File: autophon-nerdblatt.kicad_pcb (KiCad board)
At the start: 2 copper layers, 265 x 50.6 mm, 96 parts, among them J1 Conn_01x06_Female, J101 board-edge-connector, Q300 BSS84, Q301 BSS84, Q302 BSS84, Q303 BSS84, Q304 BSS84, Q305 BSS84, SW1 SW_Push, SW2 SW_Push, U101 LM1117-3.3, U102 LM2594M-5.0, U201 SN74LV1T34, U202 SN74LV1T34, U203 74AHCT595, U204 SN74LV1T34, U205 74AHCT595, U206 ESP32-WROOM-32, U207 74AHCT595, U300 L298HN, U301 L298HN, U302 L298HN

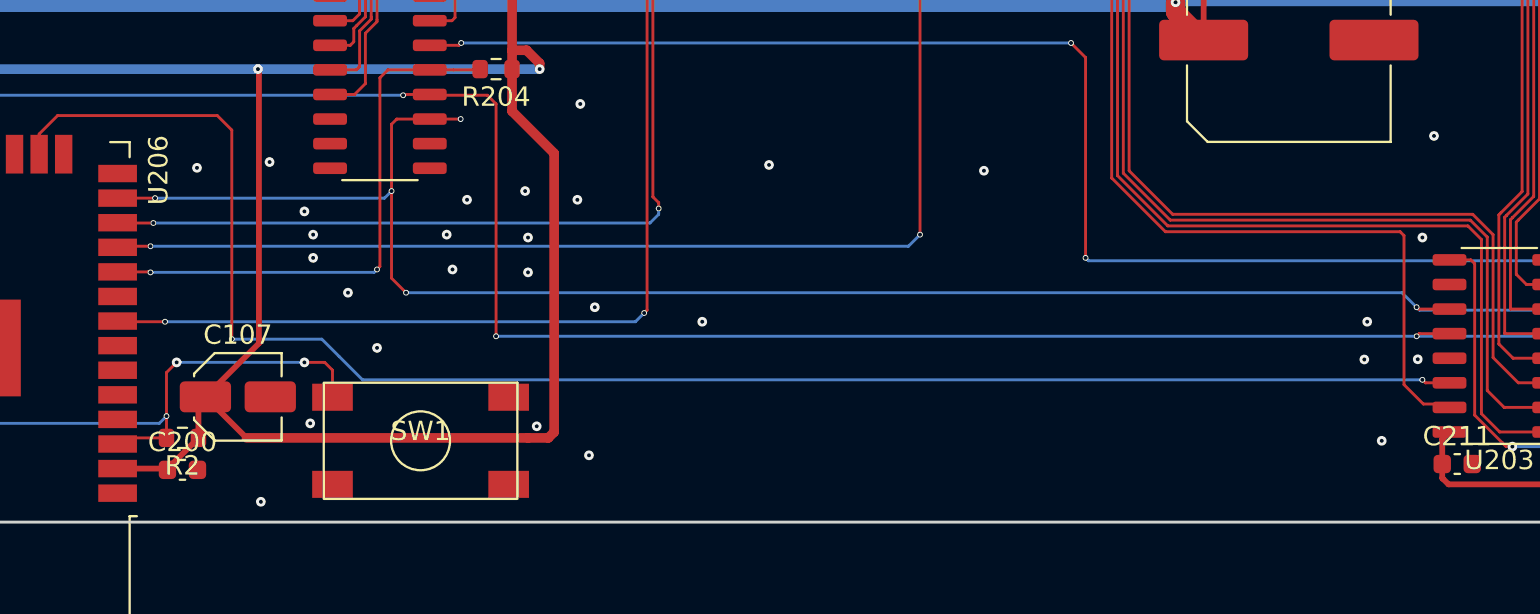
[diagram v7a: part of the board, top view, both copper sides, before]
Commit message: Add external connector, and swapped ESP pins.
Pins for motor enable, hallsensor enable and
readback of hall-sensors have been moved to
more appropriate pins.

(2 to input only, and the enable pins to
 gpios with no interesting auxiliary functions)
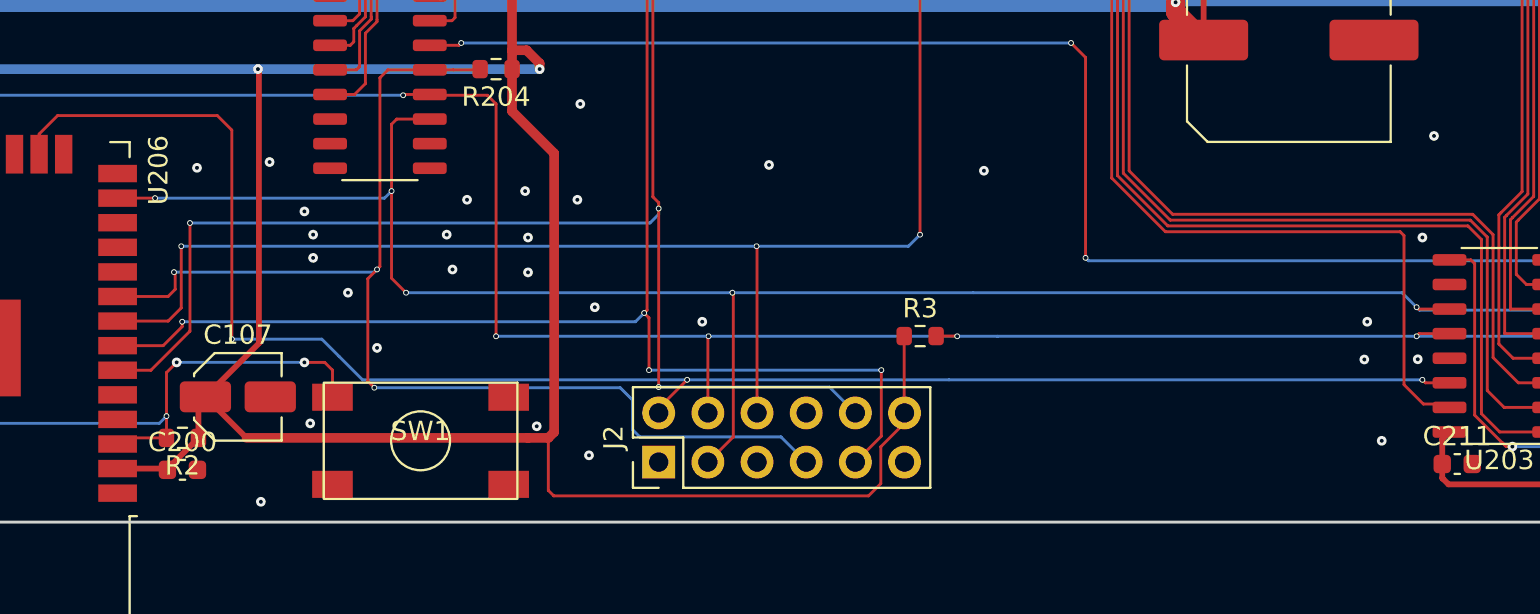
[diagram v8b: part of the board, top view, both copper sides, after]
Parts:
- added J2: Conn_02x06_Odd_Even, Connector_PinHeader_2.54mm:PinHeader_2x06_P2.54mm_Vertical, F.Cu at (225.0, 125.0)
- added R3: 10k, Resistor_SMD:R_0603_1608Metric, F.Cu at (238.5, 118.5)
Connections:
- net Net-(U206-Pad27) renamed /ESP32_Shiftregs/UART2_RXD
- net Net-(U206-Pad28) renamed /ESP32_Shiftregs/UART2_TXD
- net Net-(U206-Pad29) renamed /ESP32_Shiftregs/~VSPICS0~
- net Net-(U206-Pad30) renamed /ESP32_Shiftregs/VSPICLK
- net Net-(U206-Pad31) renamed /ESP32_Shiftregs/VSPIQ
- net Net-(U206-Pad33) renamed /ESP32_Shiftregs/I2C_SDA
- net Net-(U206-Pad36) renamed /ESP32_Shiftregs/I2C_SCL
- net Net-(U206-Pad37) renamed /ESP32_Shiftregs/VSPID
- net SPI_CIPO renamed /ESP32_Shiftregs/SPI_CIPO
- net SPI_CLK renamed /ESP32_Shiftregs/SPI_CLK
- net SPI_COPI renamed /ESP32_Shiftregs/SPI_COPI
- J101 pad 12A: no_connect_96 -> no_connect_95
- J101 pad 13A: no_connect_97 -> no_connect_96
- J101 pad 14A: no_connect_98 -> no_connect_97
- J101 pad 15A: no_connect_99 -> no_connect_98
- J101 pad 15B: no_connect_100 -> no_connect_99
- J101 pad 16A: no_connect_101 -> no_connect_100
- J101 pad 16B: no_connect_102 -> no_connect_101
- J101 pad 17A: no_connect_103 -> no_connect_102
- J101 pad 18A: no_connect_104 -> no_connect_103
- J101 pad 19A: no_connect_105 -> no_connect_104
- J101 pad 1A: no_connect_106 -> no_connect_105
- J101 pad 1B: no_connect_107 -> no_connect_106
- J101 pad 20A: no_connect_108 -> no_connect_107
- J101 pad 21A: no_connect_109 -> no_connect_108
- J101 pad 21B: no_connect_110 -> no_connect_109
- J101 pad 22A: no_connect_111 -> no_connect_110
- J101 pad 22B: no_connect_112 -> no_connect_111
- J101 pad 23B: no_connect_113 -> no_connect_112
- J101 pad 24B: no_connect_114 -> no_connect_113
- J101 pad 25B: no_connect_115 -> no_connect_114
- J101 pad 26A: no_connect_116 -> no_connect_115
- J101 pad 26B: no_connect_117 -> no_connect_116
- J101 pad 27B: no_connect_118 -> no_connect_117
- J101 pad 28B: no_connect_119 -> no_connect_118
- J101 pad 29B: no_connect_120 -> no_connect_119
- J101 pad 2A: no_connect_121 -> no_connect_120
- J101 pad 2B: no_connect_122 -> no_connect_121
- J101 pad 30A: no_connect_123 -> no_connect_122
- J101 pad 30B: no_connect_124 -> no_connect_123
- J101 pad 31B: no_connect_125 -> no_connect_124
- J101 pad 32B: no_connect_126 -> no_connect_125
- J101 pad 33B: no_connect_127 -> no_connect_126
- J101 pad 34A: no_connect_128 -> no_connect_127
- J101 pad 36B: no_connect_129 -> no_connect_128
- J101 pad 38A: no_connect_130 -> no_connect_129
- J101 pad 38B: no_connect_131 -> no_connect_130
- J101 pad 39A: no_connect_132 -> no_connect_131
- J101 pad 3A: no_connect_133 -> no_connect_132
- J101 pad 3B: no_connect_134 -> no_connect_133
- J101 pad 40A: no_connect_135 -> no_connect_134
- J101 pad 40B: no_connect_136 -> no_connect_135
- J101 pad 41A: no_connect_137 -> no_connect_136
- J101 pad 41B: no_connect_138 -> no_connect_137
- J101 pad 42A: no_connect_139 -> no_connect_138
- J101 pad 42B: no_connect_140 -> no_connect_139
- J101 pad 43A: no_connect_141 -> no_connect_140
- J101 pad 43B: no_connect_142 -> no_connect_141
- J101 pad 44A: no_connect_143 -> no_connect_142
- J101 pad 44B: no_connect_144 -> no_connect_143
- J101 pad 4A: no_connect_145 -> no_connect_144
- J101 pad 4B: no_connect_146 -> no_connect_145
- J101 pad 5A: no_connect_147 -> no_connect_146
- J101 pad 5B: no_connect_148 -> no_connect_147
- J101 pad 6B: no_connect_149 -> no_connect_148
- J101 pad 7A: no_connect_150 -> no_connect_149
- J101 pad 7B: no_connect_151 -> no_connect_150
- J101 pad 8B: no_connect_152 -> no_connect_151
- J101 pad 9A: no_connect_153 -> no_connect_152
- U206 pad 10: /ESP32_Shiftregs/~HALL_EN_3V~ -> Net-(U206-Pad10)
- U206 pad 11: /ESP32_Shiftregs/MOT_EN_3V -> Net-(U206-Pad11)
- U206 pad 12: /ESP32_Shiftregs/HALL_ROTOR_3V -> Net-(U206-Pad12)
- U206 pad 17: no_connect_154 -> no_connect_153
- U206 pad 18: no_connect_155 -> no_connect_154
- U206 pad 19: no_connect_156 -> no_connect_155
- U206 pad 20: no_connect_157 -> no_connect_156
- U206 pad 21: no_connect_158 -> no_connect_157
- U206 pad 22: no_connect_159 -> no_connect_158
- U206 pad 24: Net-(U206-Pad24) -> no_connect_159
- U206 pad 6: Net-(U206-Pad6) -> /ESP32_Shiftregs/HALL_ROTOR_3V
- U206 pad 7: Net-(U206-Pad7) -> /ESP32_Shiftregs/HALL_INDEX_3V
- U206 pad 8: /ESP32_Shiftregs/HALL_INDEX_3V -> /ESP32_Shiftregs/MOT_EN_3V
- U206 pad 9: Net-(U206-Pad9) -> /ESP32_Shiftregs/~HALL_EN_3V~
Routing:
- net /ESP32_Shiftregs/~HALL_EN_3V~: track 29.0 -> 61.2 mm, vias 2 -> 3
- net VCC: track 224.7 -> 253.1 mm
- net /ESP32_Shiftregs/HALL_ROTOR_3V: track 52.5 -> 78.9 mm, vias 2 -> 3
- net /ESP32_Shiftregs/HALL_INDEX_3V: track 63.2 -> 84.2 mm, vias 2 -> 4
- net /ESP32_Shiftregs/MOT_EN_3V: track 60.4 -> 72.5 mm, vias 2 -> 3
- net /ESP32_Shiftregs/SPI_CLK: track 106.6 -> 114.3 mm
- net /ESP32_Shiftregs/~SPI_CSO~: track 122.1 -> 127.2 mm, vias 5 -> 7
- net /ESP32_Shiftregs/SPI_COPI: track 86.3 -> 88.7 mm, vias 2 -> 3
